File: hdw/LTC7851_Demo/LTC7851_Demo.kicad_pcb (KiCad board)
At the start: 4 copper layers, 100 x 50 mm, 209 parts, among them J1101 FG_LOAD, J1102 ISNS, J1401 VOUT, J1402 LOOP_TAP, J1403 Wave_Gen_In, J201 +12V IN, J206 GND IN, J301 CLKOUT, J302 RUN, J303 SMOD, J304 IAVG, J901 +5V OUT, J902 +5V OUT, J903 GND OUT, J904 GND OUT, Q1101 BSC123N10LSGATMA1, Q1102 BSC123N10LSGATMA1, Q1201 BSC123N10LSGATMA1, Q1202 BSC123N10LSGATMA1, Q1301 BSC123N10LSGATMA1, Q1302 BSC123N10LSGATMA1, Q201 BSC123N10LSGATMA1, Q202 BSC123N10LSGATMA1, T1401 1:1 Pulse Transformer, U1101 LT1010DD, U201 LTC4365DDB, U202 74LVC1G06, U301 LTC7851UHH, U302 74LVC1G17, U303 74LVC1G06, U304 74LVC1G06, U401 SiC779, U501 SiC779, U601 SiC779, U701 SiC779, U801 LM1117-ADJ

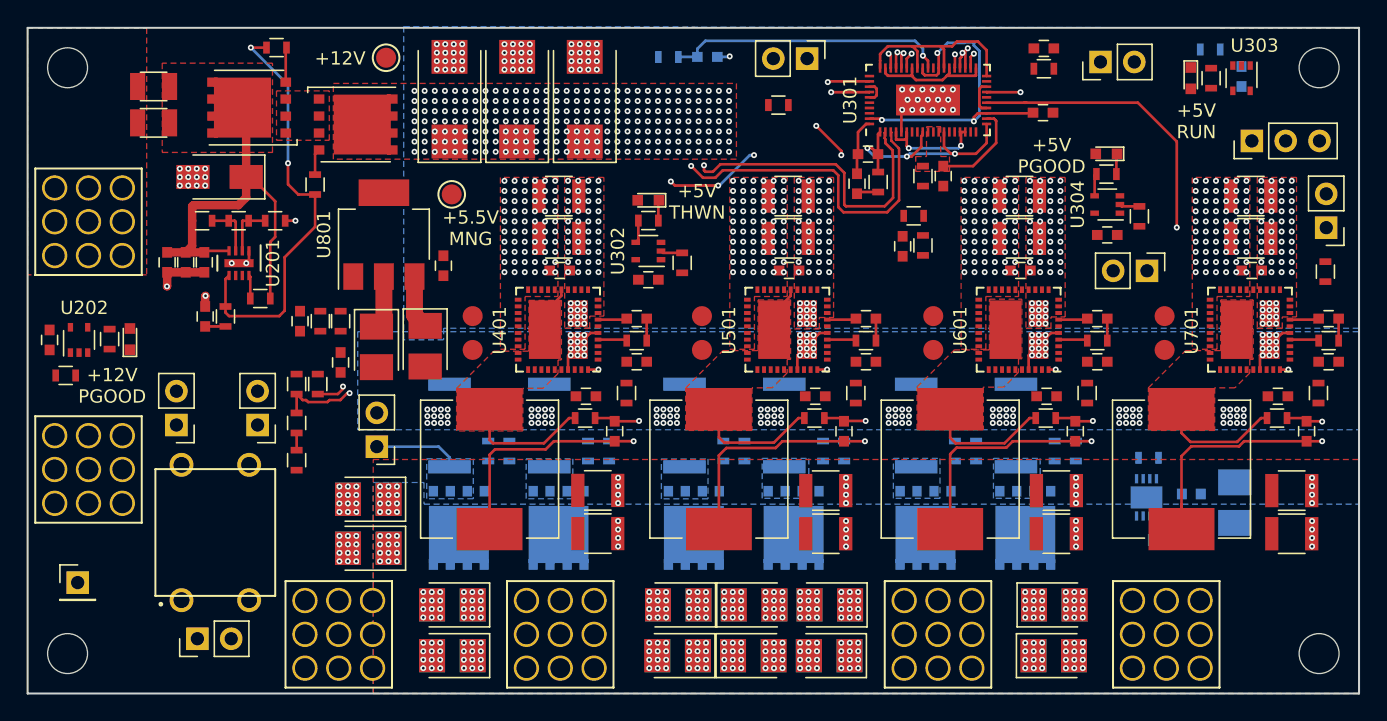
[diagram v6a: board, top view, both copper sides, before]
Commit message: More routing, removed GL ang GH phase test points
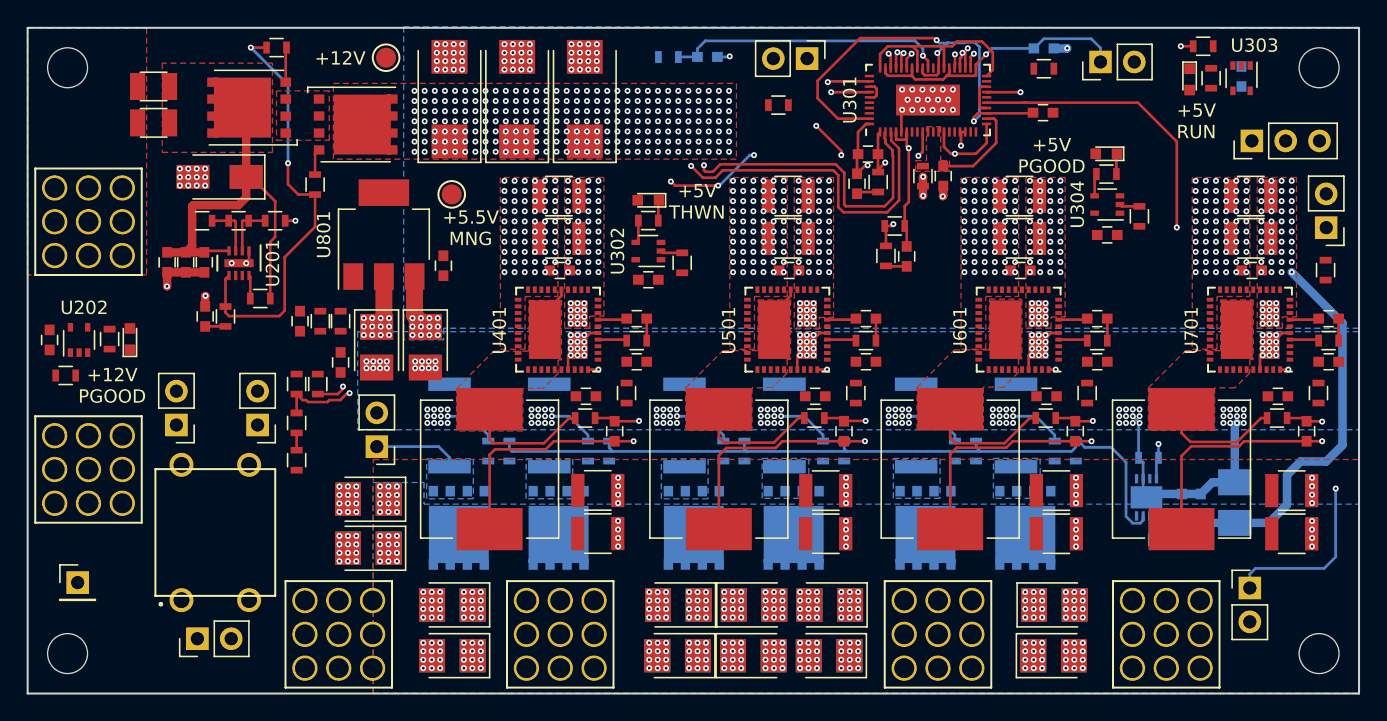
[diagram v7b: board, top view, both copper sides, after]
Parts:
- removed TP401, TP402, TP501, TP502, TP601, TP602, TP701, TP702: TP, Measurement_Points:Measurement_Point_Round-SMD-Pad_Small
- C402: moved to B.Cu
- R310: moved to F.Cu
- moved J1101 25.0 mm to (169.2, 109.4), turned to 0 degrees
- moved R402 2.89 mm to (141.8, 84.4)
- moved R404 1.61 mm to (142.5, 82.2), turned to 180 degrees
- moved C403 0.82 mm to (143.4, 84.5)
- moved R310 0.59 mm to (165.7, 68.7)
- moved D302 0.13 mm to (164.6, 71.2)
- moved R309 0.12 mm to (174.9, 85.5)
- moved C801 0.08 mm to (107.2, 91.3)
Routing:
- net LOAD_GATE: track 0.00 -> 57.7 mm
- net GND: track 24.1 -> 73.2 mm, vias 643 -> 662
- net +12V: track 4.04 -> 38.9 mm, vias 432 -> 444
- net Net-(J1101-Pad1): track 0.00 -> 31.1 mm, vias 0 -> 2
- net POS5_IAVG: track 9.35 -> 21.1 mm, vias 0 -> 1
- net POS5_SS: track 25.5 -> 34.7 mm
- net Net-(C404-Pad2): track 4.27 -> 12.8 mm, vias 0 -> 2
- net POS5_VOSNS: track 8.62 -> 16.2 mm
- net +5V: track 238.8 -> 241.0 mm
- net POS5_COMP: track 19.9 -> 17.7 mm
- net /POS5 Phase 2/POS5_ISNS2_+: track 41.2 -> 43.3 mm
- net Net-(R1102-Pad2): track 0.00 -> 1.83 mm
- net Net-(C403-Pad2): track 0.00 -> 1.58 mm
- net +5.5V_MNG: track 3.99 -> 5.42 mm, vias 0 -> 14
- net POS5_ILIM: track 15.2 -> 15.7 mm
- added copper zone on PWR, net +5.5V_MNG

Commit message: Resolved mounting hole ref des issue
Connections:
- U401 pad 36: Net-(TP402-Pad1) -> (no net)
- U401 pad 6: Net-(TP401-Pad1) -> (no net)
- U501 pad 36: Net-(TP502-Pad1) -> (no net)
- U501 pad 6: Net-(TP501-Pad1) -> (no net)
- U601 pad 36: Net-(TP602-Pad1) -> (no net)
- U601 pad 6: Net-(TP601-Pad1) -> (no net)
- U701 pad 36: Net-(TP702-Pad1) -> (no net)
- U701 pad 6: Net-(TP701-Pad1) -> (no net)
